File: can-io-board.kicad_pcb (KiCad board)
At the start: 2 copper layers, 16.4 x 20.1 mm, 22 parts, among them J1 CONN_IO, J2 CONN_PWM, U1 STM32F302K8U6, U2 MCP1703, U3 MAX3051, X1 16MHz 10ppm

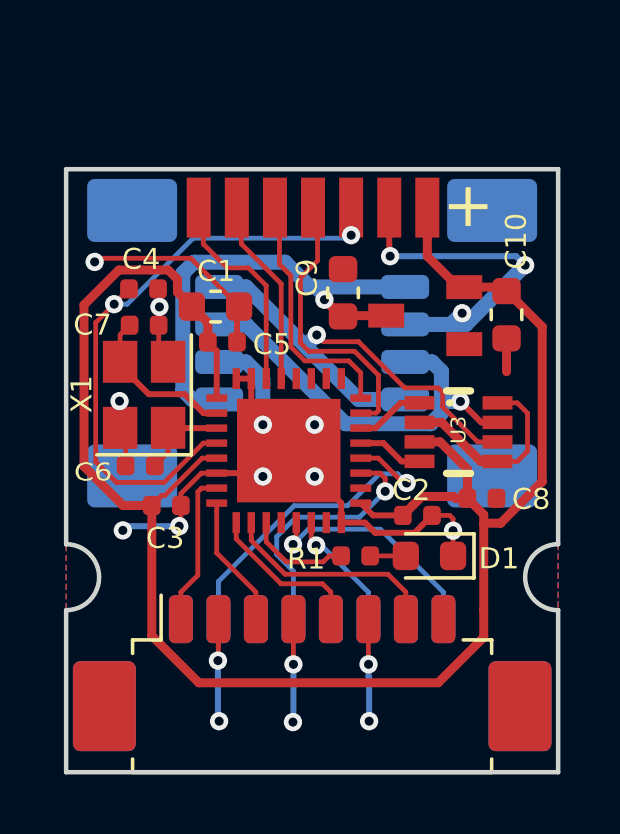
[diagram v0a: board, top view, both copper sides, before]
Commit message: Capacitor spacing
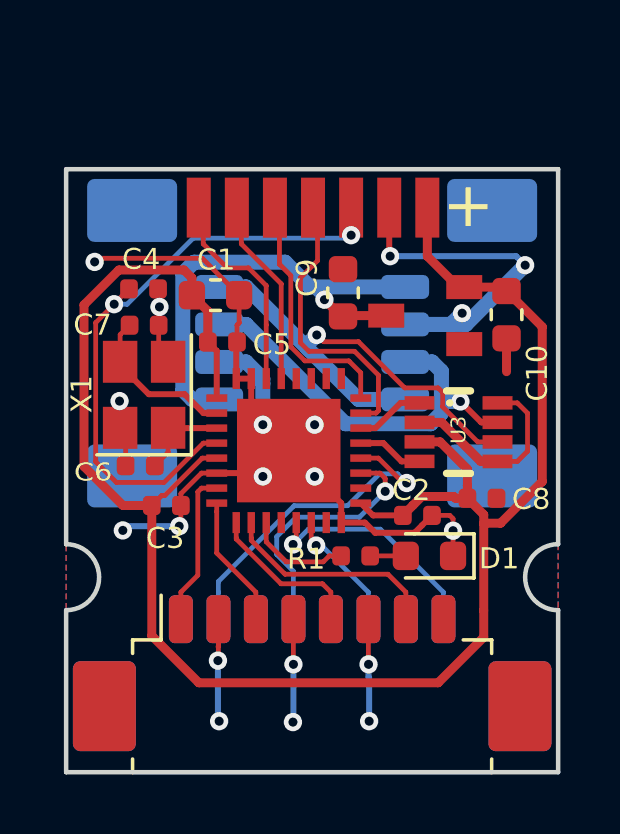
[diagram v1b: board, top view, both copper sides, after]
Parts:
- moved C1 0.38 mm to (88.8, 68.4)
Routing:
- net GND: track 61.9 -> 63.4 mm
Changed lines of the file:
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@@
     (thickness 1.6)
     (drawings 14)
-    (tracks 299)
+    (tracks 301)
     (zones 0)
     (modules 22)
@@
   )
   (setup
-    (last_trace_width 0.16)
+    (last_trace_width 0.2)
     (user_trace_width 0.2)
     (user_trace_width 0.3)
@@
   )
   (module Capacitor_SMD:C_0603_1608Metric (layer F.Cu)
-    (at 88.78 68.78)
+    (at 88.78 68.4)
     (descr "Capacitor SMD 0603 (1608 Metric), square (rectangular) end terminal, IPC_7351 nominal, (Body size source: http://www.tortai-tech.com/upload/download/2011102023233369053.pdf), generated with kicad-footprint-generator")
     (tags capacitor)
@@
     (tags capacitor)
     (attr smd)
-    (fp_text reference C10 (at -2.45 -0.32 90) (layer F.SilkS)
+    (fp_text reference C10 (at 1.95 -1.02 90) (layer F.SilkS)
       (effects (font (size 0.7 0.7) (thickness 0.15)))
     )
@@
   (gr_line (start 100.2 64.2) (end 100.2 76.7) (layer Edge.Cuts) (width 0.15))
   (gr_line (start 83.8 64.2) (end 100.2 64.2) (layer Edge.Cuts) (width 0.15))
-  (segment (start 88.525 69.3125) (end 87.9925 68.78) (width 0.3) (layer F.Cu) (net 1))
-  (segment (start 88.525 69.96) (end 88.525 69.3125) (width 0.3) (layer F.Cu) (net 1))
   (segment (start 97.175 74.197998) (end 97.175 74.75) (width 0.3) (layer F.Cu) (net 1))
   (segment (start 96.267002 73.29) (end 97.175 74.197998) (width 0.3) (layer F.Cu) (net 1))
@@
   (segment (start 86.989168 75.075832) (end 87.091146 75.075832) (width 0.16) (layer F.Cu) (net 1))
   (segment (start 86.655 75.41) (end 86.989168 75.075832) (width 0.16) (layer F.Cu) (net 1))
-  (segment (start 85.695421 75.41) (end 86.655 75.41) (width 0.3) (layer F.Cu) (net 1))
-  (segment (start 84.394989 74.109568) (end 85.695421 75.41) (width 0.3) (layer F.Cu) (net 1))
-  (segment (start 84.394989 68.722993) (end 84.394989 74.109568) (width 0.3) (layer F.Cu) (net 1))
-  (segment (start 87.509999 68.297499) (end 87.509999 67.867981) (width 0.3) (layer F.Cu) (net 1))
-  (segment (start 85.557992 67.55999) (end 84.394989 68.722993) (width 0.3) (layer F.Cu) (net 1))
-  (segment (start 87.202008 67.55999) (end 85.557992 67.55999) (width 0.3) (layer F.Cu) (net 1))
-  (segment (start 87.509999 67.867981) (end 87.202008 67.55999) (width 0.3) (layer F.Cu) (net 1))
-  (segment (start 87.9925 68.78) (end 87.509999 68.297499) (width 0.3) (layer F.Cu) (net 1))
   (segment (start 97.72 75.715) (end 97.175 75.17) (width 0.3) (layer F.Cu) (net 1))
   (segment (start 97.72 76.02) (end 97.72 75.715) (width 0.3) (layer F.Cu) (net 1))
@@
   (segment (start 88.82 70.255) (end 88.525 69.96) (width 0.2) (layer F.Cu) (net 1))
   (segment (start 88.82 71.83) (end 88.82 70.255) (width 0.2) (layer F.Cu) (net 1))
+  (segment (start 84.394989 74.109568) (end 85.695421 75.41) (width 0.3) (layer F.Cu) (net 1))
+  (segment (start 84.394989 68.722993) (end 84.394989 74.109568) (width 0.3) (layer F.Cu) (net 1))
+  (segment (start 85.557992 67.55999) (end 84.394989 68.722993) (width 0.3) (layer F.Cu) (net 1))
+  (segment (start 87.72749 67.55999) (end 85.557992 67.55999) (width 0.3) (layer F.Cu) (net 1))
+  (segment (start 87.9925 67.825) (end 87.72749 67.55999) (width 0.3) (layer F.Cu) (net 1))
+  (segment (start 85.695421 75.41) (end 86.655 75.41) (width 0.3) (layer F.Cu) (net 1))
+  (segment (start 87.9925 68.4) (end 87.9925 67.825) (width 0.3) (layer F.Cu) (net 1))
+  (segment (start 88.525 68.9325) (end 87.9925 68.4) (width 0.3) (layer F.Cu) (net 1))
+  (segment (start 88.525 69.96) (end 88.525 68.9325) (width 0.3) (layer F.Cu) (net 1))
   (segment (start 97.618444 73.94) (end 98.18 73.94) (width 0.3) (layer F.Cu) (net 2))
   (segment (start 96.318444 72.64) (end 97.618444 73.94) (width 0.3) (layer F.Cu) (net 2))
@@
   (segment (start 86.885 69.4) (end 86.885 68.815) (width 0.16) (layer F.Cu) (net 2))
   (via (at 84.75 67.29) (size 0.61) (drill 0.3) (layers F.Cu B.Cu) (net 2))
-  (segment (start 84.87002 67.16998) (end 84.75 67.29) (width 0.16) (layer F.Cu) (net 2))
-  (segment (start 87.95748 67.16998) (end 84.87002 67.16998) (width 0.16) (layer F.Cu) (net 2))
-  (segment (start 89.5675 68.78) (end 87.95748 67.16998) (width 0.16) (layer F.Cu) (net 2))
   (segment (start 96.6975 75.8475) (end 96.59 75.74) (width 0.16) (layer F.Cu) (net 2))
   (segment (start 95.995 75.74) (end 96.59 75.74) (width 0.16) (layer F.Cu) (net 2))
@@
   (segment (start 93.875 80.7) (end 93.88 80.705) (width 0.16) (layer F.Cu) (net 2))
   (segment (start 93.875 79.2) (end 93.875 80.7) (width 0.16) (layer F.Cu) (net 2))
-  (segment (start 89.495 68.8525) (end 89.5675 68.78) (width 0.2) (layer F.Cu) (net 2))
-  (segment (start 89.495 69.96) (end 89.495 68.8525) (width 0.2) (layer F.Cu) (net 2))
   (segment (start 89.47 71.18) (end 89.97 71.18) (width 0.2) (layer F.Cu) (net 2))
   (via (at 91.36 82.63) (size 0.61) (drill 0.3) (layers F.Cu B.Cu) (net 2))
@@
   (segment (start 96.625 69.375) (end 97 69) (width 0.5) (layer B.Cu) (net 2))
   (segment (start 95.1 69.375) (end 96.625 69.375) (width 0.5) (layer B.Cu) (net 2))
+  (segment (start 88.33748 67.16998) (end 89.5675 68.4) (width 0.16) (layer F.Cu) (net 2))
+  (segment (start 84.87002 67.16998) (end 88.33748 67.16998) (width 0.16) (layer F.Cu) (net 2))
+  (segment (start 84.75 67.29) (end 84.87002 67.16998) (width 0.16) (layer F.Cu) (net 2))
+  (segment (start 89.5675 69.3275) (end 89.5675 68.4) (width 0.16) (layer F.Cu) (net 2))
+  (segment (start 89.495 69.4) (end 89.5675 69.3275) (width 0.16) (layer F.Cu) (net 2))
+  (segment (start 89.495 69.96) (end 89.495 69.4) (width 0.16) (layer F.Cu) (net 2))
+  (segment (start 89.47 69.985) (end 89.495 69.96) (width 0.2) (layer F.Cu) (net 2))
+  (segment (start 89.47 71.18) (end 89.47 69.985) (width 0.2) (layer F.Cu) (net 2))
   (via (at 93.3 66.4) (size 0.61) (drill 0.3) (layers F.Cu B.Cu) (net 3))
   (segment (start 93.3 66.4) (end 93.3 65.48) (width 0.16) (layer F.Cu) (net 3))

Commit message: Improved GND connection, solder mask clearance
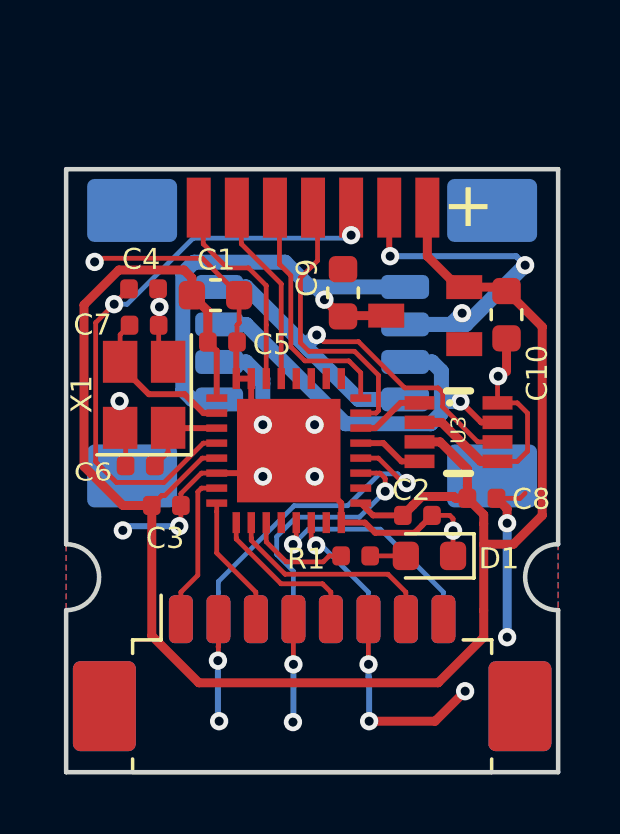
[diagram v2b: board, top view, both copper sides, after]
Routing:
- net GND: track 63.4 -> 73.7 mm, vias 19 -> 23
- net VCC: track 62.2 -> 63.1 mm
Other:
- rule pad_to_mask_clearance: 0.2 -> 0.15
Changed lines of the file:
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@@
     (thickness 1.6)
     (drawings 14)
-    (tracks 301)
+    (tracks 314)
     (zones 0)
     (modules 22)
@@
   )
   (setup
-    (last_trace_width 0.2)
+    (last_trace_width 0.16)
     (user_trace_width 0.2)
     (user_trace_width 0.3)
@@
     (user_trace_width 0.5)
     (trace_clearance 0.16)
-    (zone_clearance 0.17)
+    (zone_clearance 0.25)
     (zone_45_only no)
     (trace_min 0.1525)
@@
     (pad_size 1.524 1.524)
     (pad_drill 0.762)
-    (pad_to_mask_clearance 0.2)
+    (pad_to_mask_clearance 0.15)
     (solder_mask_min_width 0.25)
     (aux_axis_origin 0 0)
@@
   (segment (start 98.3475 68.13) (end 98.48 68.2625) (width 0.3) (layer F.Cu) (net 1))
   (segment (start 97.07 68.13) (end 98.3475 68.13) (width 0.3) (layer F.Cu) (net 1))
-  (segment (start 98.282018 76) (end 97.74 76) (width 0.3) (layer F.Cu) (net 1))
-  (segment (start 97.74 76) (end 97.72 76.02) (width 0.3) (layer F.Cu) (net 1))
-  (segment (start 99.67 69.4525) (end 99.67 74.612018) (width 0.3) (layer F.Cu) (net 1))
-  (segment (start 99.67 74.612018) (end 98.282018 76) (width 0.3) (layer F.Cu) (net 1))
-  (segment (start 98.48 68.2625) (end 99.67 69.4525) (width 0.3) (layer F.Cu) (net 1))
-  (segment (start 97.72 78.91) (end 97.72 76.02) (width 0.3) (layer F.Cu) (net 1))
   (segment (start 97.72 79.8) (end 97.72 78.91) (width 0.3) (layer F.Cu) (net 1))
   (segment (start 96.2 81.32) (end 97.72 79.8) (width 0.3) (layer F.Cu) (net 1))
@@
   (segment (start 88.525 68.9325) (end 87.9925 68.4) (width 0.3) (layer F.Cu) (net 1))
   (segment (start 88.525 69.96) (end 88.525 68.9325) (width 0.3) (layer F.Cu) (net 1))
+  (segment (start 98.710202 76.7) (end 97.72 76.7) (width 0.3) (layer F.Cu) (net 1))
+  (segment (start 99.67 75.740202) (end 98.710202 76.7) (width 0.3) (layer F.Cu) (net 1))
+  (segment (start 99.67 69.4525) (end 99.67 75.740202) (width 0.3) (layer F.Cu) (net 1))
+  (segment (start 98.48 68.2625) (end 99.67 69.4525) (width 0.3) (layer F.Cu) (net 1))
+  (segment (start 97.72 76.7) (end 97.72 76.02) (width 0.3) (layer F.Cu) (net 1))
+  (segment (start 97.72 78.91) (end 97.72 76.7) (width 0.3) (layer F.Cu) (net 1))
   (segment (start 97.618444 73.94) (end 98.18 73.94) (width 0.3) (layer F.Cu) (net 2))
   (segment (start 96.318444 72.64) (end 97.618444 73.94) (width 0.3) (layer F.Cu) (net 2))
@@
   (segment (start 89.47 69.985) (end 89.495 69.96) (width 0.2) (layer F.Cu) (net 2))
   (segment (start 89.47 71.18) (end 89.47 69.985) (width 0.2) (layer F.Cu) (net 2))
+  (segment (start 98.5 75.525) (end 98.5 76) (width 0.3) (layer F.Cu) (net 2))
+  (via (at 98.5 76) (size 0.61) (drill 0.3) (layers F.Cu B.Cu) (net 2))
+  (segment (start 98.145 75.17) (end 98.5 75.525) (width 0.3) (layer F.Cu) (net 2))
+  (via (at 98.5 79.8) (size 0.61) (drill 0.3) (layers F.Cu B.Cu) (net 2))
+  (segment (start 98.5 76) (end 98.5 79.8) (width 0.3) (layer B.Cu) (net 2))
+  (via (at 97.1 81.6) (size 0.61) (drill 0.3) (layers F.Cu B.Cu) (net 2))
+  (segment (start 96.1 82.6) (end 97.1 81.6) (width 0.3) (layer F.Cu) (net 2))
+  (segment (start 93.9 82.6) (end 96.1 82.6) (width 0.3) (layer F.Cu) (net 2))
+  (segment (start 98.145 75.17) (end 98.93 75.17) (width 0.16) (layer F.Cu) (net 2))
+  (segment (start 98.93 75.17) (end 99.1 75) (width 0.16) (layer F.Cu) (net 2))
+  (via (at 98.2 71.1) (size 0.61) (drill 0.3) (layers F.Cu B.Cu) (net 2))
+  (segment (start 98.18 71.12) (end 98.2 71.1) (width 0.16) (layer F.Cu) (net 2))
+  (segment (start 98.18 71.99) (end 98.18 71.12) (width 0.16) (layer F.Cu) (net 2))
   (via (at 93.3 66.4) (size 0.61) (drill 0.3) (layers F.Cu B.Cu) (net 3))
   (segment (start 93.3 66.4) (end 93.3 65.48) (width 0.16) (layer F.Cu) (net 3))
@@
   (segment (start 93.935 77.09) (end 95.1225 77.09) (width 0.16) (layer F.Cu) (net 24))
   (zone (net 2) (net_name GND) (layer F.Cu) (hatch edge 0.508)
-    (connect_pads (clearance 0.17))
+    (connect_pads (clearance 0.25))
     (min_thickness 0.17)
     (fill yes (arc_segments 16) (thermal_gap 0.3) (thermal_bridge_width 0.3))
@@
   )
   (zone (net 2) (net_name GND) (layer B.Cu) (hatch edge 0.508)
-    (connect_pads (clearance 0.17))
+    (connect_pads (clearance 0.25))
     (min_thickness 0.17)
     (fill yes (arc_segments 16) (thermal_gap 0.3) (thermal_bridge_width 0.3))

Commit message: Silkscreen placement
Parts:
- CONN1: footprint _connectors:_Solder_Pad1.27_7 -> Connector_Molex:Molex_PicoBlade_53048-1410_1x07_P1.25mm_Horizontal
- moved CONN1 3.73 mm to (95.8, 65.2)
- moved G*** 3.52 mm to (92.0, 70.4), turned to 180 degrees
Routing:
- net GND: track 73.7 -> 77.7 mm
- net /SWCK: track 7.72 -> 8.70 mm
- net /IO_PB6_I2C1SCL_UART1TX: track 5.64 -> 6.61 mm
- net /SWIO: track 8.99 -> 9.82 mm
- net /IO_PB7_I2C1SDA_UART1RX: track 6.38 -> 6.92 mm

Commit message: Add CAN reverse voltage protection diode
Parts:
- added D2: SBR130S3-7, Diode_SMD:D_SOD-323_HandSoldering, F.Cu at (93.7, 69.3)
- moved C9 1.50 mm to (94.4, 67.7), turned to 180 degrees
- moved C10 1.45 mm to (98.5, 70.5), turned to 180 degrees
- moved U2 1.08 mm to (97.4, 69.0), turned to 0 degrees
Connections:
- C9 pad 1: /5V_CAN -> Net-(C9-Pad1)
- U2 pad 3: /5V_CAN -> Net-(C9-Pad1)
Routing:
- net GND: track 77.7 -> 84.4 mm, vias 23 -> 18
- net Net-(C9-Pad1): track 0.00 -> 5.52 mm
- net /5V_CAN: track 16.1 -> 14.5 mm
- net VCC: track 63.3 -> 64.2 mm
- net /IO_PB7_I2C1SDA_UART1RX: track 6.92 -> 7.56 mm
- net /RST: track 21.2 -> 20.6 mm, vias 2 -> 1
